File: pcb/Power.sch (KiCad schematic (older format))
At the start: 5 parts, among them P5 CONN_02X10, U3 TLV70233DBV

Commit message: v3 of f3fc. Correct mosfet pinout. Add measurement points. Remove MPU. Tweaked pinout with one less SPI.
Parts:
- removed D4: D_Schottky_x2_KCom_AKA, Housings_SOT-23_SOT-143_TSOT-6:SOT-23_Handsoldering, symbol D_Schottky_x2_KCom_AKA
- added D4: D_Schottky_x2_KCom_AAK, Housings_SOT-23_SOT-143_TSOT-6:SOT-23_Handsoldering, symbol D_Schottky_x2_KCom_AAK
- added D5: PWR, LEDs:LED-0603, symbol LED
- added P1: 3V3, Measurement_Points:Measurement_Point_Round-SMD-Pad_Small, symbol CONN_01X01
- added P8: GND, Measurement_Points:Measurement_Point_Square-SMD-Pad_Small, symbol CONN_01X01
- added P9: 5V, Measurement_Points:Measurement_Point_Round-SMD-Pad_Small, symbol CONN_01X01
- added R12: 1k, Resistors_SMD:R_0603_HandSoldering, symbol R_Small
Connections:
- wire segments 32 -> 35
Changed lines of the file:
@@
 LIBS:ti-regu
 LIBS:ti-power-mux
+LIBS:FlightController-cache
 EELAYER 25 0
 EELAYER END
@@
 $EndDescr
 $Comp
-L +5VA #PWR036
+L +5VA #PWR029
 U 1 1 563342DB
 P 7750 2800
-F 0 "#PWR036" H 7750 2650 50  0001 C CNN
+F 0 "#PWR029" H 7750 2650 50  0001 C CNN
 F 1 "+5VA" H 7750 2940 50  0000 C CNN
 F 2 "" H 7750 2800 60  0000 C CNN
@@
 USB Power
 $Comp
-L +5V #PWR037
+L +5V #PWR030
 U 1 1 56334305
 P 3350 2100
-F 0 "#PWR037" H 3350 1950 50  0001 C CNN
+F 0 "#PWR030" H 3350 1950 50  0001 C CNN
 F 1 "+5V" H 3350 2240 50  0000 C CNN
 F 2 "" H 3350 2100 60  0000 C CNN
@@
 $EndComp
 $Comp
-L VDD #PWR038
+L VDD #PWR031
 U 1 1 5633432D
 P 7300 4050
-F 0 "#PWR038" H 7300 3900 50  0001 C CNN
+F 0 "#PWR031" H 7300 3900 50  0001 C CNN
 F 1 "VDD" H 7300 4200 50  0000 C CNN
 F 2 "" H 7300 4050 60  0000 C CNN
@@
 $EndComp
 $Comp
-L GNDPWR #PWR039
+L GNDPWR #PWR032
 U 1 1 56334341
 P 7750 5100
-F 0 "#PWR039" H 7750 4900 50  0001 C CNN
+F 0 "#PWR032" H 7750 4900 50  0001 C CNN
 F 1 "GNDPWR" H 7750 4970 50  0000 C CNN
 F 2 "" H 7750 5050 60  0000 C CNN
@@
 	5950 3500 5950 4400
 Wire Wire Line
-	7000 4300 7300 4300
+	7000 4300 8500 4300
 Wire Wire Line
 	7300 4050 7300 4400
@@
 	7750 3300 7500 3300
 $Comp
-L PWR_FLAG #FLG040
+L PWR_FLAG #FLG033
 U 1 1 5634570D
 P 3700 2150
-F 0 "#FLG040" H 3700 2245 50  0001 C CNN
+F 0 "#FLG033" H 3700 2245 50  0001 C CNN
 F 1 "PWR_FLAG" H 3700 2330 50  0000 C CNN
 F 2 "" H 3700 2150 60  0000 C CNN
@@
 $EndComp
 $Comp
-L +5V #PWR041
+L +5V #PWR034
 U 1 1 5634F1D6
 P 6900 2600
-F 0 "#PWR041" H 6900 2450 50  0001 C CNN
+F 0 "#PWR034" H 6900 2450 50  0001 C CNN
 F 1 "+5V" H 6900 2740 50  0000 C CNN
 F 2 "" H 6900 2600 60  0000 C CNN
@@
 $EndComp
 Wire Wire Line
-	4350 4700 7750 4700
+	4350 4700 7850 4700
 Wire Wire Line
 	4350 2750 4350 4700
@@
 Connection ~ 3550 2750
 $Comp
-L +BATT #PWR042
+L +BATT #PWR035
 U 1 1 5634F8B8
 P 3300 3550
-F 0 "#PWR042" H 3300 3400 50  0001 C CNN
+F 0 "#PWR035" H 3300 3400 50  0001 C CNN
 F 1 "+BATT" H 3300 3690 50  0000 C CNN
 F 2 "" H 3300 3550 60  0000 C CNN
@@
 $EndComp
 $Comp
-L PWR_FLAG #FLG043
+L PWR_FLAG #FLG036
 U 1 1 5637C30C
 P 2900 3550
-F 0 "#FLG043" H 2900 3645 50  0001 C CNN
+F 0 "#FLG036" H 2900 3645 50  0001 C CNN
 F 1 "PWR_FLAG" H 2900 3730 50  0000 C CNN
 F 2 "" H 2900 3550 60  0000 C CNN
@@
 Wire Wire Line
 	6550 4700 6550 4650
-$Comp
-L D_Schottky_x2_KCom_AKA D4
-U 1 1 563D391A
-P 7200 3300
-F 0 "D4" H 7250 3200 50  0000 C CNN
-F 1 "D_Schottky_x2_KCom_AKA" H 7200 3400 50  0000 C CNN
-F 2 "Housings_SOT-23_SOT-143_TSOT-6:SOT-23_Handsoldering" H 7200 3300 60  0001 C CNN
-F 3 "" H 7200 3300 60  0000 C CNN
-	1    7200 3300
-	1    0    0    -1
-$EndComp
 Wire Wire Line
 	7200 3500 5950 3500
 $Comp
-L PWR_FLAG #FLG044
+L PWR_FLAG #FLG037
 U 1 1 5637C41B
 P 4550 4050
-F 0 "#FLG044" H 4550 4145 50  0001 C CNN
+F 0 "#FLG037" H 4550 4145 50  0001 C CNN
 F 1 "PWR_FLAG" H 4550 4230 50  0000 C CNN
 F 2 "" H 4550 4050 60  0000 C CNN
@@
 	1    0    0    -1
 $EndComp
+$Comp
+L CONN_01X01 P1
+U 1 1 5654FA4D
+P 8150 4100
+F 0 "P1" H 8150 4200 50  0000 C CNN
+F 1 "3V3" V 8250 4100 50  0000 C CNN
+F 2 "Measurement_Points:Measurement_Point_Round-SMD-Pad_Small" H 8150 4100 60  0001 C CNN
+F 3 "" H 8150 4100 60  0000 C CNN
+	1    8150 4100
+	0    -1   -1   0
+$EndComp
+$Comp
+L D_Schottky_x2_KCom_AAK D4
+U 1 1 5654FAE8
+P 7200 3300
+F 0 "D4" H 7250 3200 50  0000 C CNN
+F 1 "D_Schottky_x2_KCom_AAK" H 7200 3400 50  0000 C CNN
+F 2 "Housings_SOT-23_SOT-143_TSOT-6:SOT-23_Handsoldering" H 7200 3300 60  0001 C CNN
+F 3 "" H 7200 3300 60  0000 C CNN
+	1    7200 3300
+	1    0    0    -1
+$EndComp
+$Comp
+L R_Small R12
+U 1 1 565552F2
+P 7950 4700
+F 0 "R12" H 7980 4720 50  0000 L CNN
+F 1 "1k" H 7980 4660 50  0000 L CNN
+F 2 "Resistors_SMD:R_0603_HandSoldering" H 7950 4700 60  0001 C CNN
+F 3 "" H 7950 4700 60  0000 C CNN
+	1    7950 4700
+	0    1    1    0
+$EndComp
+$Comp
+L LED D5
+U 1 1 5655531F
+P 8300 4700
+F 0 "D5" H 8300 4800 50  0000 C CNN
+F 1 "PWR" H 8300 4600 50  0000 C CNN
+F 2 "LEDs:LED-0603" H 8300 4700 60  0001 C CNN
+F 3 "" H 8300 4700 60  0000 C CNN
+	1    8300 4700
+	1    0    0    -1
+$EndComp
+Connection ~ 7750 4700
+Wire Wire Line
+	8050 4700 8100 4700
+Wire Wire Line
+	8500 4300 8500 4700
+Connection ~ 8150 4300
+$Comp
+L CONN_01X01 P9
+U 1 1 56555904
+P 5950 3300
+F 0 "P9" H 5950 3400 50  0000 C CNN
+F 1 "5V" V 6050 3300 50  0000 C CNN
+F 2 "Measurement_Points:Measurement_Point_Round-SMD-Pad_Small" H 5950 3300 60  0001 C CNN
+F 3 "" H 5950 3300 60  0000 C CNN
+	1    5950 3300
+	0    -1   -1   0
+$EndComp
+$Comp
+L CONN_01X01 P8
+U 1 1 56555995
+P 5100 4300
+F 0 "P8" H 5100 4400 50  0000 C CNN
+F 1 "GND" V 5200 4300 50  0000 C CNN
+F 2 "Measurement_Points:Measurement_Point_Square-SMD-Pad_Small" H 5100 4300 60  0001 C CNN
+F 3 "" H 5100 4300 60  0000 C CNN
+	1    5100 4300
+	0    -1   -1   0
+$EndComp
+Wire Wire Line
+	5100 4500 5100 4700
+Connection ~ 5100 4700
 $EndSCHEMATC

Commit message: v5 of F3FC. Adjusts motor output location, switches to MPU-6000 and adds chickadee logo back.
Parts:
- removed P8: GND, Measurement_Points:Measurement_Point_Square-SMD-Pad_Small, symbol CONN_01X01
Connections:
- wire segments 35 -> 34
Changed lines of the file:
@@
 $EndDescr
 $Comp
-L +5VA #PWR035
+L +5VA #PWR032
 U 1 1 563342DB
 P 7750 2800
-F 0 "#PWR035" H 7750 2650 50  0001 C CNN
+F 0 "#PWR032" H 7750 2650 50  0001 C CNN
 F 1 "+5VA" H 7750 2940 50  0000 C CNN
 F 2 "" H 7750 2800 60  0000 C CNN
@@
 USB Power
 $Comp
-L +5V #PWR036
+L +5V #PWR033
 U 1 1 56334305
 P 3350 2100
-F 0 "#PWR036" H 3350 1950 50  0001 C CNN
+F 0 "#PWR033" H 3350 1950 50  0001 C CNN
 F 1 "+5V" H 3350 2240 50  0000 C CNN
 F 2 "" H 3350 2100 60  0000 C CNN
@@
 $EndComp
 $Comp
-L VDD #PWR037
+L VDD #PWR034
 U 1 1 5633432D
 P 7300 4050
-F 0 "#PWR037" H 7300 3900 50  0001 C CNN
+F 0 "#PWR034" H 7300 3900 50  0001 C CNN
 F 1 "VDD" H 7300 4200 50  0000 C CNN
 F 2 "" H 7300 4050 60  0000 C CNN
@@
 $EndComp
 $Comp
-L GNDPWR #PWR038
+L GNDPWR #PWR035
 U 1 1 56334341
 P 7750 5100
-F 0 "#PWR038" H 7750 4900 50  0001 C CNN
+F 0 "#PWR035" H 7750 4900 50  0001 C CNN
 F 1 "GNDPWR" H 7750 4970 50  0000 C CNN
 F 2 "" H 7750 5050 60  0000 C CNN
@@
 	7750 3300 7500 3300
 $Comp
-L PWR_FLAG #FLG039
+L PWR_FLAG #FLG036
 U 1 1 5634570D
 P 3700 2150
-F 0 "#FLG039" H 3700 2245 50  0001 C CNN
+F 0 "#FLG036" H 3700 2245 50  0001 C CNN
 F 1 "PWR_FLAG" H 3700 2330 50  0000 C CNN
 F 2 "" H 3700 2150 60  0000 C CNN
@@
 $EndComp
 $Comp
-L +5V #PWR040
+L +5V #PWR037
 U 1 1 5634F1D6
 P 6900 2600
-F 0 "#PWR040" H 6900 2450 50  0001 C CNN
+F 0 "#PWR037" H 6900 2450 50  0001 C CNN
 F 1 "+5V" H 6900 2740 50  0000 C CNN
 F 2 "" H 6900 2600 60  0000 C CNN
@@
 Connection ~ 3550 2750
 $Comp
-L +BATT #PWR041
+L +BATT #PWR038
 U 1 1 5634F8B8
 P 3300 3550
-F 0 "#PWR041" H 3300 3400 50  0001 C CNN
+F 0 "#PWR038" H 3300 3400 50  0001 C CNN
 F 1 "+BATT" H 3300 3690 50  0000 C CNN
 F 2 "" H 3300 3550 60  0000 C CNN
@@
 $EndComp
 $Comp
-L PWR_FLAG #FLG042
+L PWR_FLAG #FLG039
 U 1 1 5637C30C
 P 2900 3550
-F 0 "#FLG042" H 2900 3645 50  0001 C CNN
+F 0 "#FLG039" H 2900 3645 50  0001 C CNN
 F 1 "PWR_FLAG" H 2900 3730 50  0000 C CNN
 F 2 "" H 2900 3550 60  0000 C CNN
@@
 	7200 3500 5950 3500
 $Comp
-L PWR_FLAG #FLG043
+L PWR_FLAG #FLG040
 U 1 1 5637C41B
 P 4550 4050
-F 0 "#FLG043" H 4550 4145 50  0001 C CNN
+F 0 "#FLG040" H 4550 4145 50  0001 C CNN
 F 1 "PWR_FLAG" H 4550 4230 50  0000 C CNN
 F 2 "" H 4550 4050 60  0000 C CNN
@@
 	0    -1   -1   0
 $EndComp
-$Comp
-L CONN_01X01 P8
-U 1 1 56555995
-P 5100 4300
-F 0 "P8" H 5100 4400 50  0000 C CNN
-F 1 "GND" V 5200 4300 50  0000 C CNN
-F 2 "Measurement_Points:Measurement_Point_Square-SMD-Pad_Small" H 5100 4300 60  0001 C CNN
-F 3 "" H 5100 4300 60  0000 C CNN
-	1    5100 4300
-	0    -1   -1   0
-$EndComp
-Wire Wire Line
-	5100 4500 5100 4700
-Connection ~ 5100 4700
 $EndSCHEMATC

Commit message: F3FC v6 which features correct reset circuitry.
Also:
* Routes USB as differential pair.
* Corrects reset circuit.
* Adds fiducials
* Matches up LED numbering to reference
* Supports current pin from power connector.
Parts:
- D4: footprint Housings_SOT-23_SOT-143_TSOT-6:SOT-23_Handsoldering -> TO_SOT_Packages_SMD:SOT-23
- D5: value PWR -> Red
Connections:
- net labels added: CURRENT
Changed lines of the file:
@@
 Connection ~ 4350 3150
-Wire Wire Line
-	3350 2750 3850 2750
 Wire Wire Line
 	3550 2750 3550 3550
@@
 Wire Wire Line
 	3700 2250 3350 2250
-Connection ~ 3550 2750
 $Comp
 L +BATT #PWR038
@@
 F 0 "D4" H 7250 3200 50  0000 C CNN
 F 1 "D_Schottky_x2_KCom_AAK" H 7200 3400 50  0000 C CNN
-F 2 "Housings_SOT-23_SOT-143_TSOT-6:SOT-23_Handsoldering" H 7200 3300 60  0001 C CNN
+F 2 "TO_SOT_Packages_SMD:SOT-23" H 7200 3300 60  0001 C CNN
 F 3 "" H 7200 3300 60  0000 C CNN
 	1    7200 3300
@@
 P 8300 4700
 F 0 "D5" H 8300 4800 50  0000 C CNN
-F 1 "PWR" H 8300 4600 50  0000 C CNN
+F 1 "Red" H 8300 4600 50  0000 C CNN
 F 2 "LEDs:LED-0603" H 8300 4700 60  0001 C CNN
 F 3 "" H 8300 4700 60  0000 C CNN
@@
 	0    -1   -1   0
 $EndComp
+Wire Wire Line
+	3350 2750 3550 2750
+Text HLabel 3850 2750 1    60   Input ~ 0
+CURRENT
 $EndSCHEMATC

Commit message: More changes to F3. Can't remember what.
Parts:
- added P8: CONN_01X01, Measurement_Points:Measurement_Point_Square-SMD-Pad_Small, symbol CONN_01X01
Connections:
- wire segments 34 -> 35
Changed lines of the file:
@@
 Text HLabel 3850 2750 1    60   Input ~ 0
 CURRENT
+$Comp
+L CONN_01X01 P8
+U 1 1 56DE4DD7
+P 5100 4400
+F 0 "P8" H 5100 4500 50  0000 C CNN
+F 1 "CONN_01X01" V 5200 4400 50  0000 C CNN
+F 2 "Measurement_Points:Measurement_Point_Square-SMD-Pad_Small" H 5100 4400 50  0001 C CNN
+F 3 "" H 5100 4400 50  0000 C CNN
+	1    5100 4400
+	0    -1   -1   0
+$EndComp
+Wire Wire Line
+	5100 4600 5100 4700
+Connection ~ 5100 4700
 $EndSCHEMATC

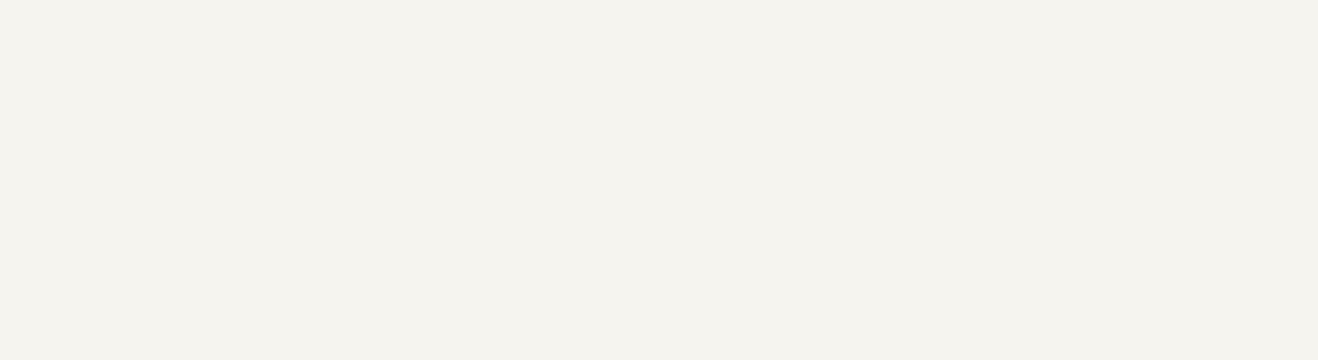
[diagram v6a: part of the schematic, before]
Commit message: Add license information to many files. PCB design files are CC-BY and code is MIT license.
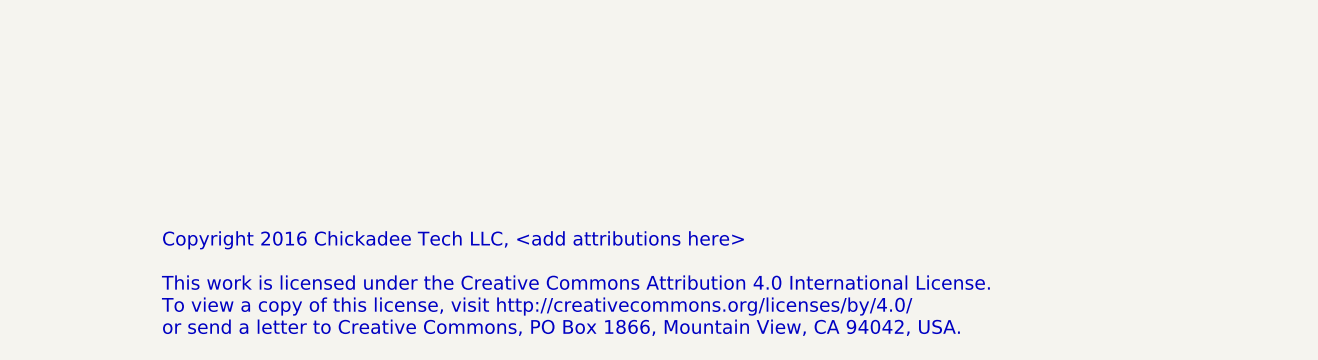
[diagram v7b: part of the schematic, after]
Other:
- note added: "Copyright 2016 Chickadee Tech LLC, <add attributions here>\n\nThis work is licensed under the Creative Commons Attribution 4.0 International License.\nTo view a copy of this license, visit http://creativecommons.org/licenses/by/4.0/\nor send a letter to Creative Commons, PO Box 1866, Mountain View, CA 94042, USA."
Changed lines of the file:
@@
 	5100 4600 5100 4700
 Connection ~ 5100 4700
+Text Notes 7000 7050 0    60   ~ 0
+Copyright 2016 Chickadee Tech LLC, <add attributions here>\n\nThis work is licensed under the Creative Commons Attribution 4.0 International License.\nTo view a copy of this license, visit http://creativecommons.org/licenses/by/4.0/\nor send a letter to Creative Commons, PO Box 1866, Mountain View, CA 94042, USA.
 $EndSCHEMATC
